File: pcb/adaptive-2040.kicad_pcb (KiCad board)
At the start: 2 copper layers, 54.4 x 80.8 mm, 24 parts, among them J1 USB_A, J10 AudioJack2, J11 AudioJack2, J12 AudioJack2, J13 AudioJack2, J14 AudioJack2, J15 AudioJack2, J16 AudioJack2, J17 AudioJack2, J18 AudioJack2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

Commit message: tidy things up a little
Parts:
- moved J11 66.7 mm to (125.3, 177.9)
- moved J12 66.7 mm to (125.3, 170.6)
- moved J16 66.7 mm to (125.3, 141.1)
- moved J1 66.7 mm to (101.5, 179.7)
- moved J13 66.7 mm to (125.3, 163.2)
- moved J15 66.7 mm to (125.3, 148.5)
- moved J17 66.7 mm to (125.3, 133.7)
- moved J18 66.7 mm to (125.3, 126.4)
- moved REF11 66.7 mm to (81.7, 111.9)
- moved REF12 66.7 mm to (128.4, 111.9)
- moved J10 66.7 mm to (84.7, 177.9)
- moved J14 66.7 mm to (125.3, 155.8)
- moved J19 66.7 mm to (125.3, 119.0)
- moved J2 66.7 mm to (84.7, 119.0)
- moved J3 66.7 mm to (84.7, 126.4)
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
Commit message: r1 board
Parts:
- moved REF13 23.3 mm to (80.6, 208.3)
- moved J1 23.3 mm to (100.6, 202.9)
- moved REF14145235 23.3 mm to (127.6, 208.3)
- moved J10 22.8 mm to (83.8, 200.7)
- moved J11 22.7 mm to (124.5, 200.7)
- moved U1 20.7 mm to (104.1, 113.4)
- moved REF11 20.5 mm to (80.6, 91.4)
- moved REF12 20.5 mm to (127.6, 91.4)
- moved J2 20.0 mm to (83.8, 99.1)
- moved J19 20.0 mm to (124.5, 99.1)
- moved J9 17.4 mm to (83.8, 188.0)
- moved J12 17.4 mm to (124.5, 188.0)
- moved J3 14.6 mm to (83.8, 111.8)
- moved J18 14.6 mm to (124.5, 111.8)
- moved J8 12.1 mm to (83.8, 175.3)
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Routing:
- net DP: track 73.8 -> 124.8 mm
- net DM: track 70.4 -> 119.5 mm
- net B3: track 42.7 -> 88.1 mm
- net VBUS: track 74.8 -> 118.8 mm, vias 2 -> 0
- net L2: track 40.5 -> 80.4 mm
- net R2: track 35.0 -> 70.3 mm
- net B4: track 59.8 -> 94.4 mm
- net B2: track 30.1 -> 62.9 mm
- net R1: track 49.5 -> 79.1 mm
- net B1: track 25.3 -> 50.0 mm
- net L1: track 43.2 -> 63.6 mm
- net S1: track 11.9 -> 32.2 mm
- net RIGHT: track 23.7 -> 42.9 mm
- net LEFT: track 18.9 -> 32.2 mm
- net R3: track 22.2 -> 12.1 mm
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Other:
- board size 54.4 x 80.8 mm -> 54.6 x 124.5 mm
- board text added: "if you want your JLCPCB order number hidden by the Pico, this is a good spot to put it"
- board text added: "r1"
- board text removed: "r0"

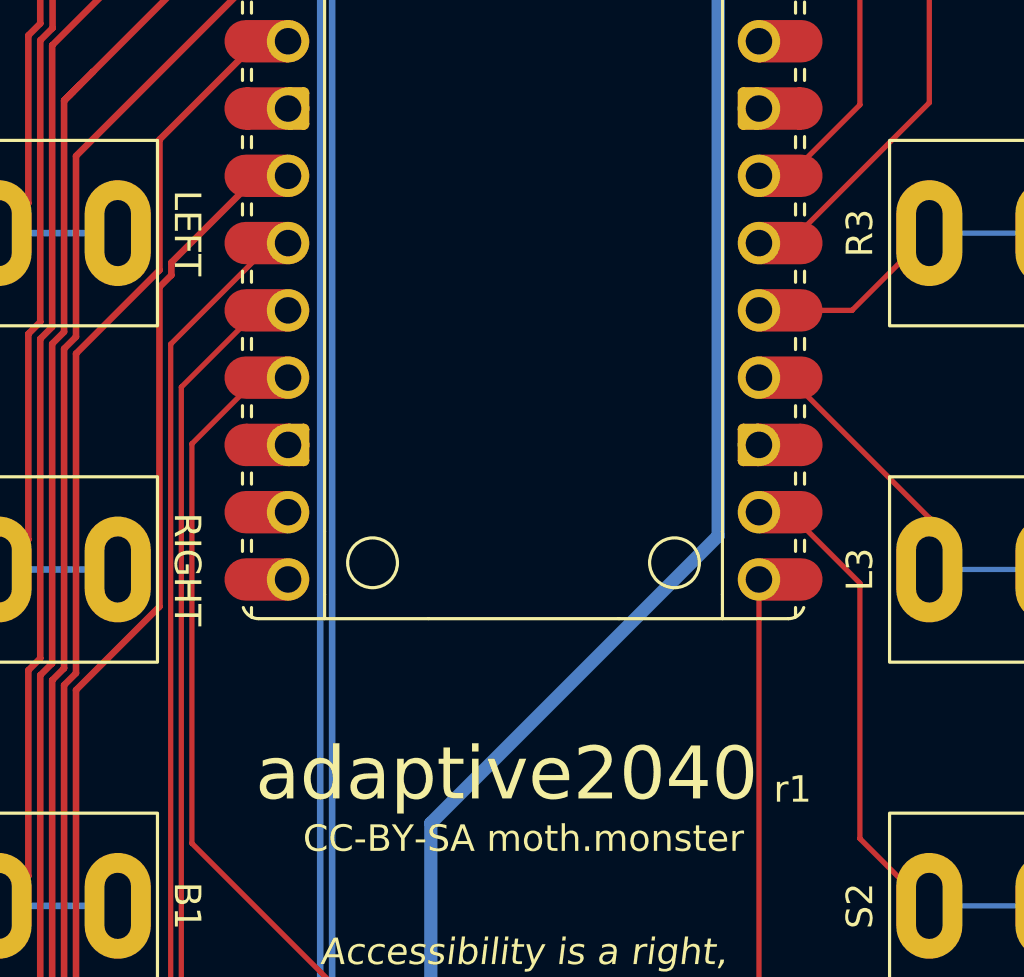
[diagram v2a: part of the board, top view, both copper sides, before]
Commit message: r1.1 - fix silkscreen error
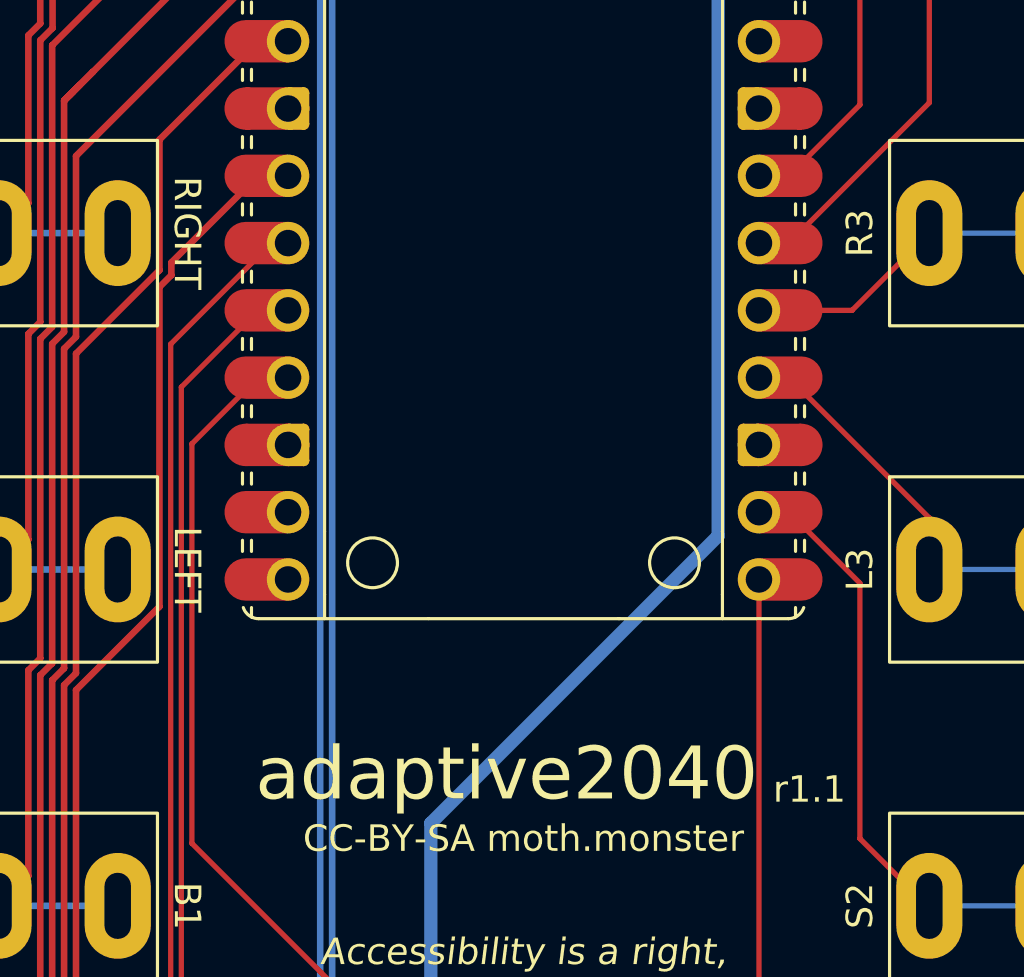
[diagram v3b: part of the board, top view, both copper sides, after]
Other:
- board text added: "r1.1"
- board text removed: "r1"
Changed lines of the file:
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@@
 	(title_block
 		(title "adaptive2040")
-		(date "2024-03-21")
-		(rev "1")
+		(date "2024-04-04")
+		(rev "1.1")
 		(company "moth.monster")
 	)
@@
 		(allow_soldermask_bridges_in_footprints no)
 		(pcbplotparams
-			(layerselection 0x00010fc_ffffffff)
+			(layerselection 0x00010e0_ffffffff)
 			(plot_on_all_layers_selection 0x0000000_00000000)
 			(disableapertmacros no)
@@
 		(fp_arc
 			(start 10.579676 25.189937)
-			(mid 10.35796 25.493961)
+			(mid 10.357949 25.493953)
 			(end 10 25.61)
 			(stroke
@@
 	)
 	(gr_text "LEFT"
-		(at 91.44 124.46 270)
+		(at 91.44 137.16 270)
 		(layer "F.SilkS")
 		(effects
@@
 		)
 	)
-	(gr_text "r1"
-		(at 114.3 146.05 0)
+	(gr_text "r1.1"
+		(at 114.935 146.05 0)
 		(layer "F.SilkS")
 		(effects
@@
 	)
 	(gr_text "RIGHT"
-		(at 91.44 137.16 270)
+		(at 91.44 124.46 270)
 		(layer "F.SilkS")
 		(effects
